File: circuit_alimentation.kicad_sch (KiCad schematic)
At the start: 33 parts, among them U1 STM32-(STM32H745ZIT6)

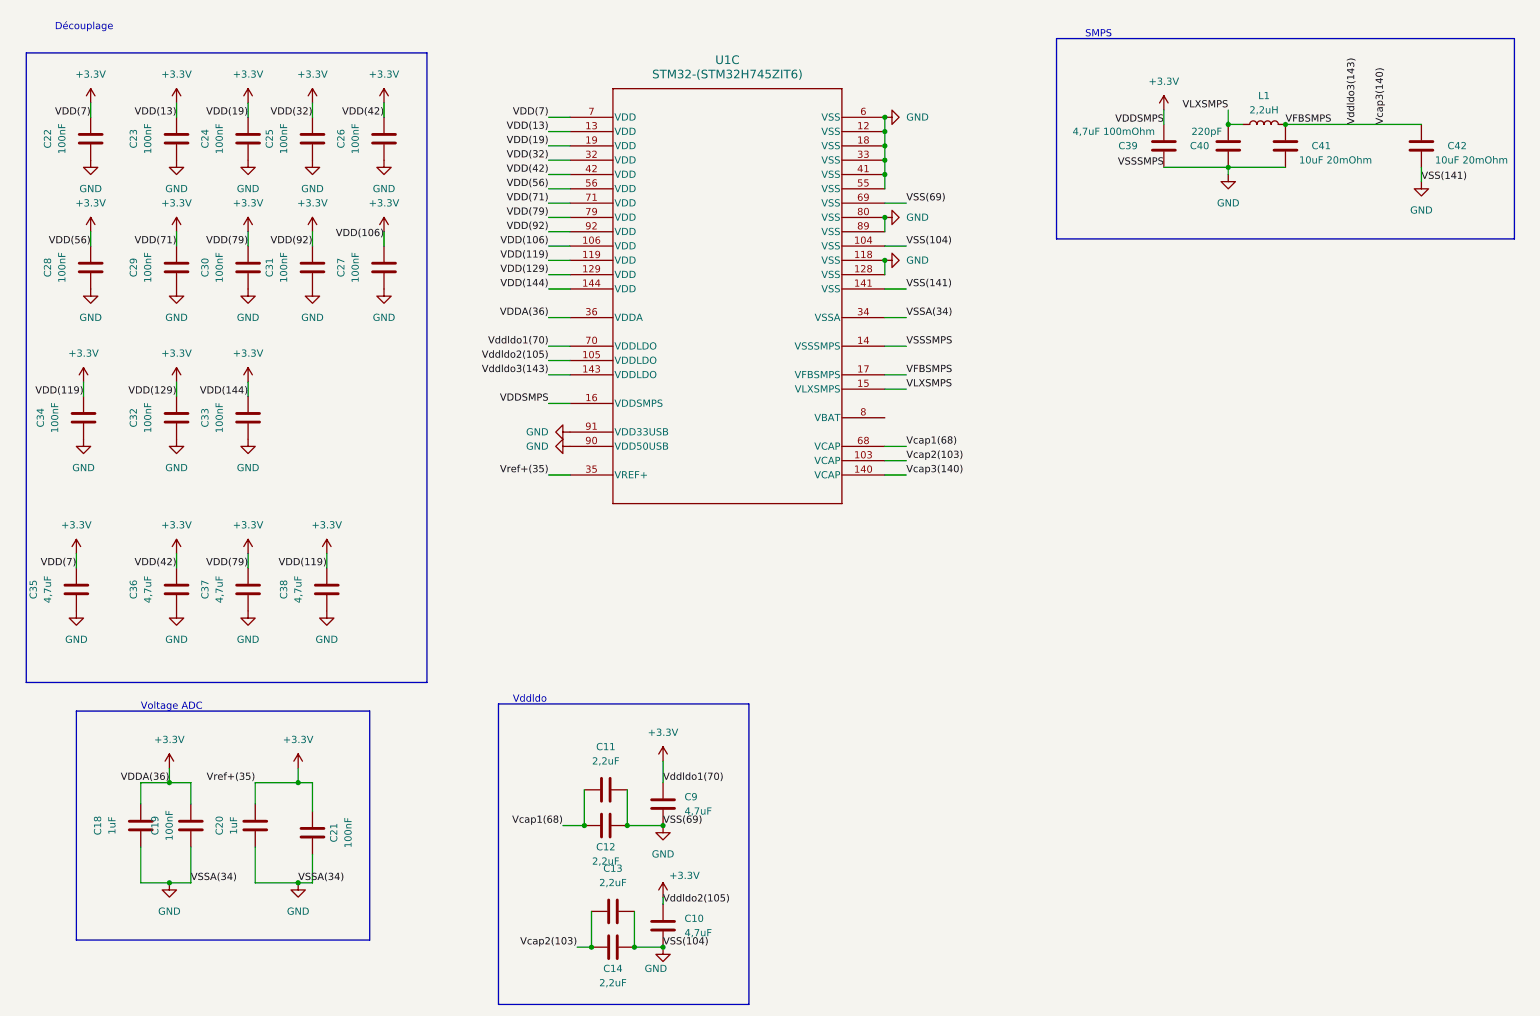
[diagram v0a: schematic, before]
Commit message: Recommit du Vbuck
On réessaye de commit parce que ça a pas marché...

Le régulateur de tension buck converter a été ajouté au payload dans la page Vbuck qui remplace la page circuit caméras.
J'ai enlevé la switch du buck et connecté l'entré on/off à GND.
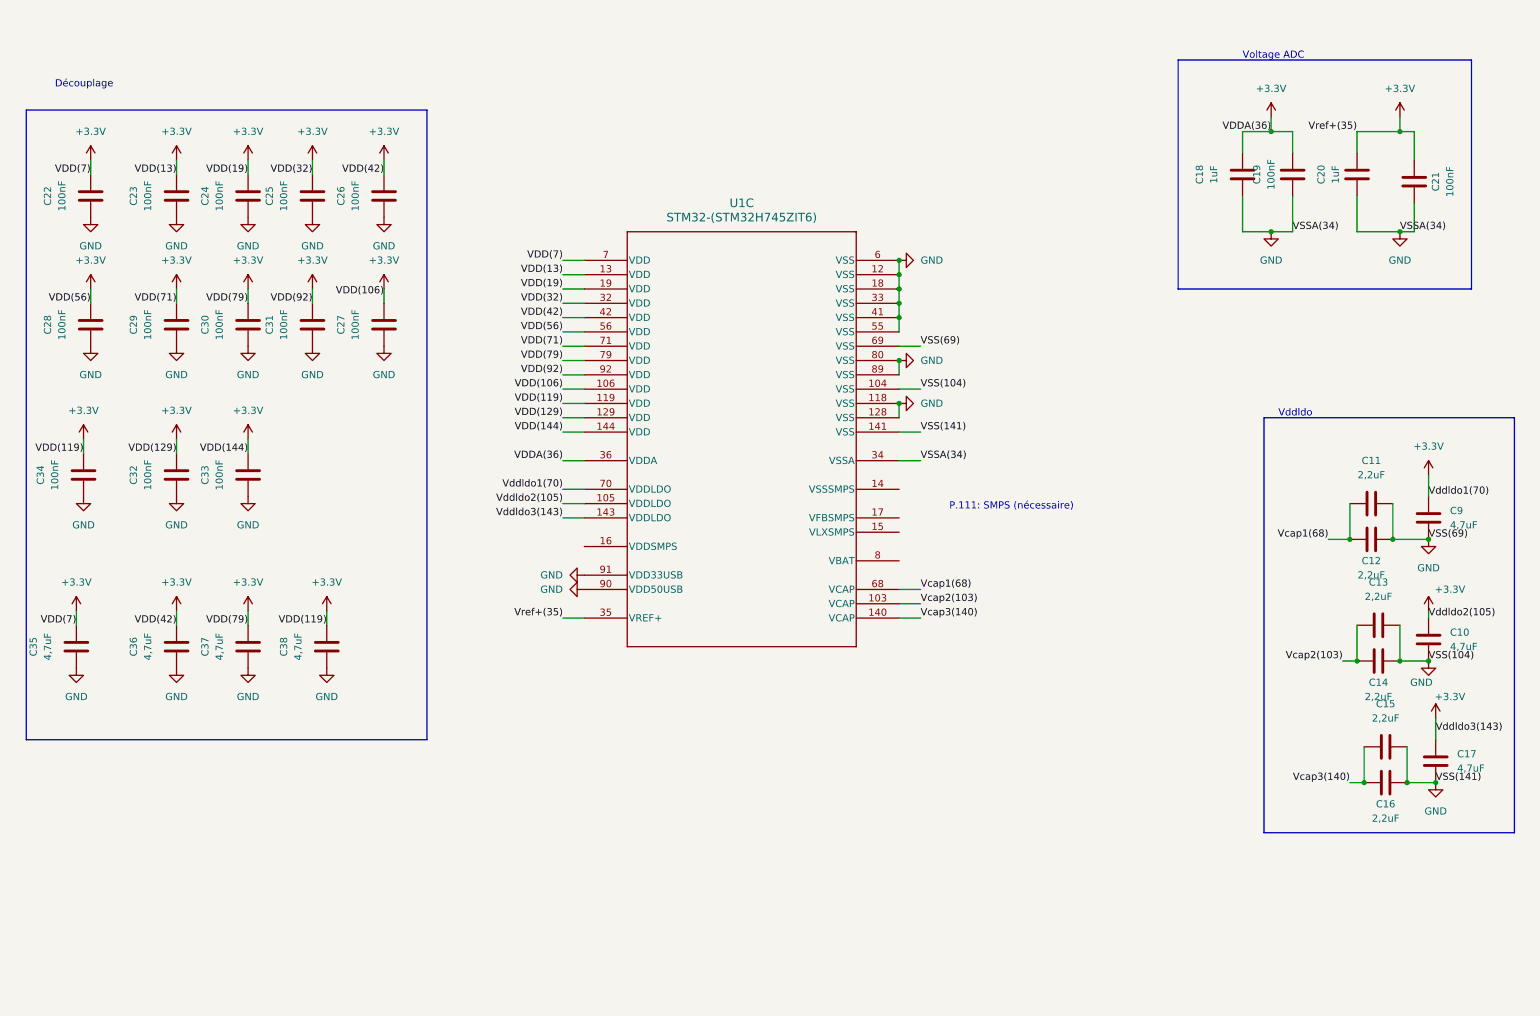
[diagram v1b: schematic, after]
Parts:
- removed C39: 4,7uF 100mOhm, symbol Device:C
- removed C40: 220pF, symbol Device:C
- removed C41, C42: 10uF 20mOhm, symbol Device:C
- removed L1: 2,2uH, symbol Device:L
- added C15, C16: 2,2uF, symbol Device:C
- added C17: 4,7uF, symbol Device:C
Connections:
- net +3.3V: now also U1.143 (VDDLDO), C17.2; no longer U1.16 (VDDSMPS)
- net GND: now also C15.2, C16.2, C17.1; no longer U1.14 (VSSSMPS)
- removed net VFBSMPS: U1.140 (VCAP), U1.143 (VDDLDO), U1.17 (VFBSMPS)
- net VLXSMPS: no longer names the net of U1.15 (VLXSMPS)
- new net Vcap3(140): C15.1, C16.1, U1.140 (VCAP)
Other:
- note added: "P.111: SMPS (nécessaire)"
- note removed: "SMPS"
- moved on the sheet: C10, C11, C12, C13, C14, C18, C19, C20, C21, C22, C23, C24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

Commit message: Revert "Recommit du Vbuck"
This reverts commit db6b1385e92bec759ec8c6f30127fdc08b8b4918.
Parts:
- removed C15, C16: 2,2uF, symbol Device:C
- removed C17: 4,7uF, symbol Device:C
- added C39: 4,7uF 100mOhm, symbol Device:C
- added C40: 220pF, symbol Device:C
- added C41, C42: 10uF 20mOhm, symbol Device:C
- added L1: 2,2uH, symbol Device:L
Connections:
- net Vcap3(140) is gone; now on net VFBSMPS: U1.140 (VCAP)
- net +3.3V: now also U1.16 (VDDSMPS), C39.1; no longer U1.143 (VDDLDO)
- net GND: now also U1.14 (VSSSMPS), C39.2, C40.2, C41.1, C42.1
- net VLXSMPS: now reaches U1.15 (VLXSMPS)
- net VLXSMPS: now also C40.1, L1.1
- net VFBSMPS: now reaches U1.17 (VFBSMPS)
- net VFBSMPS: now also U1.143 (VDDLDO), C41.2, C42.2, L1.2
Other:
- note added: "SMPS"
- note removed: "P.111: SMPS (nécessaire)"
- moved on the sheet: C10, C11, C12, C13, C14, C18, C19, C20, C21, C22, C23, C24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

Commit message: SPI_Debut
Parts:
- removed C20: 1uF, symbol Device:C
- removed C21: 100nF, symbol Device:C
- added C15: 100nF, symbol Device:C
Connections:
- net +3.3V: now also U1.8 (VBAT), C15.2
- net GND: now also C15.1

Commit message: ADC_Select
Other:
- moved on the sheet: C10, C11, C12, C13, C14, C15, C18, C19, C22, C23, C24, C25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
